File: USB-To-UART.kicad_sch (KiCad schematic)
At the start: 8 parts, among them Q1 NMOS, Q2 NMOS, U4 CH340X

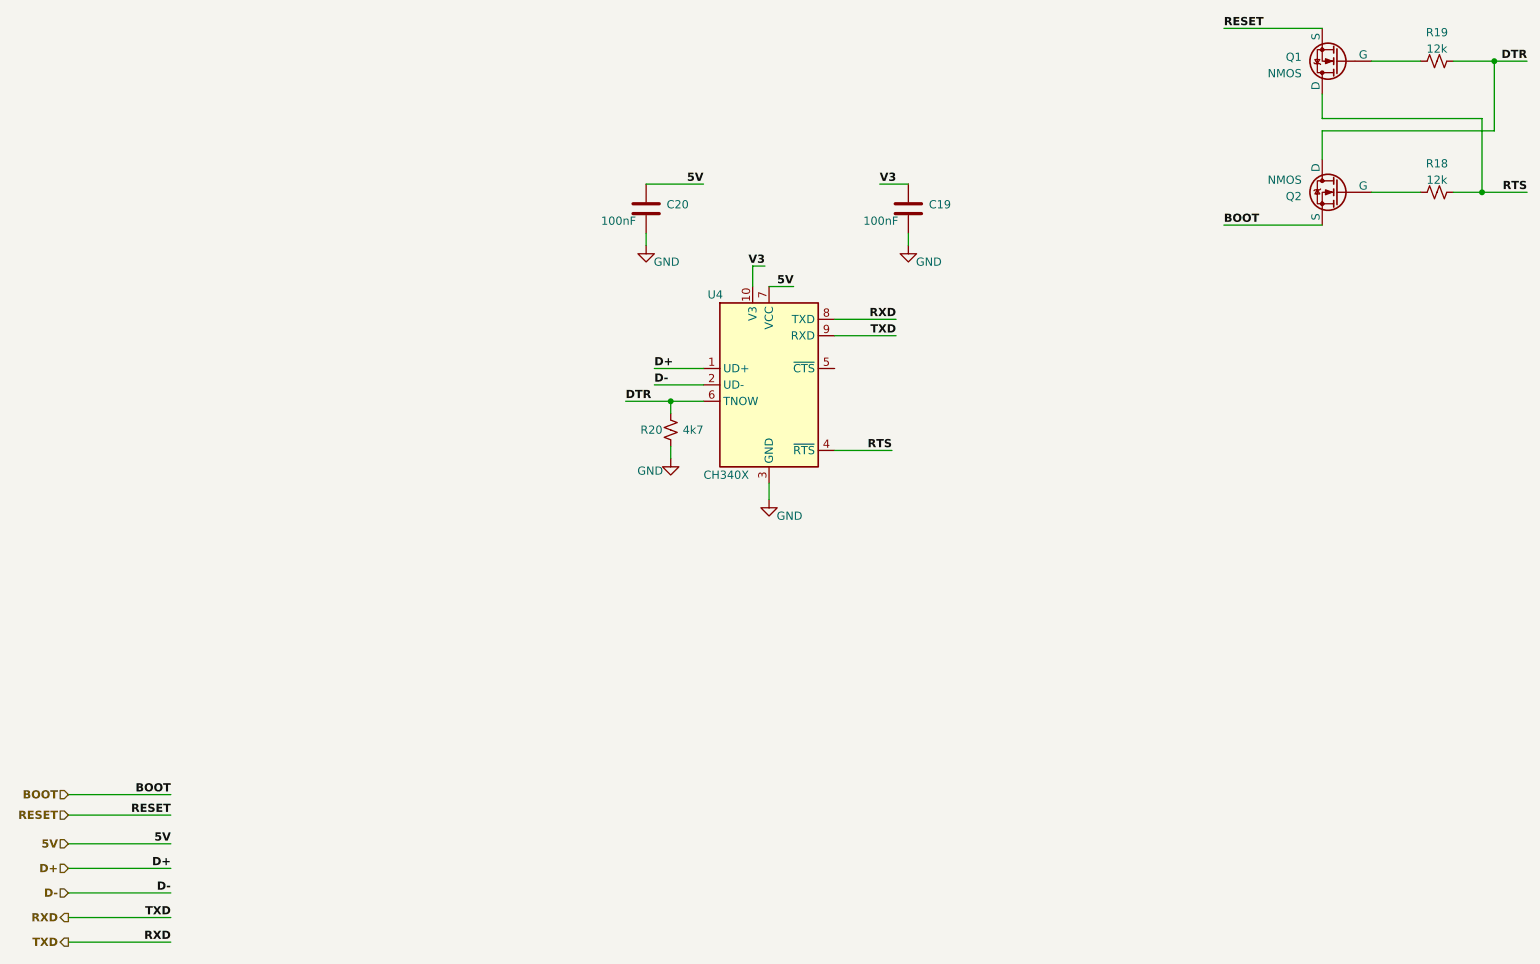
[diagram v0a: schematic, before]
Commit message: UART Tx and Rx correctly placed
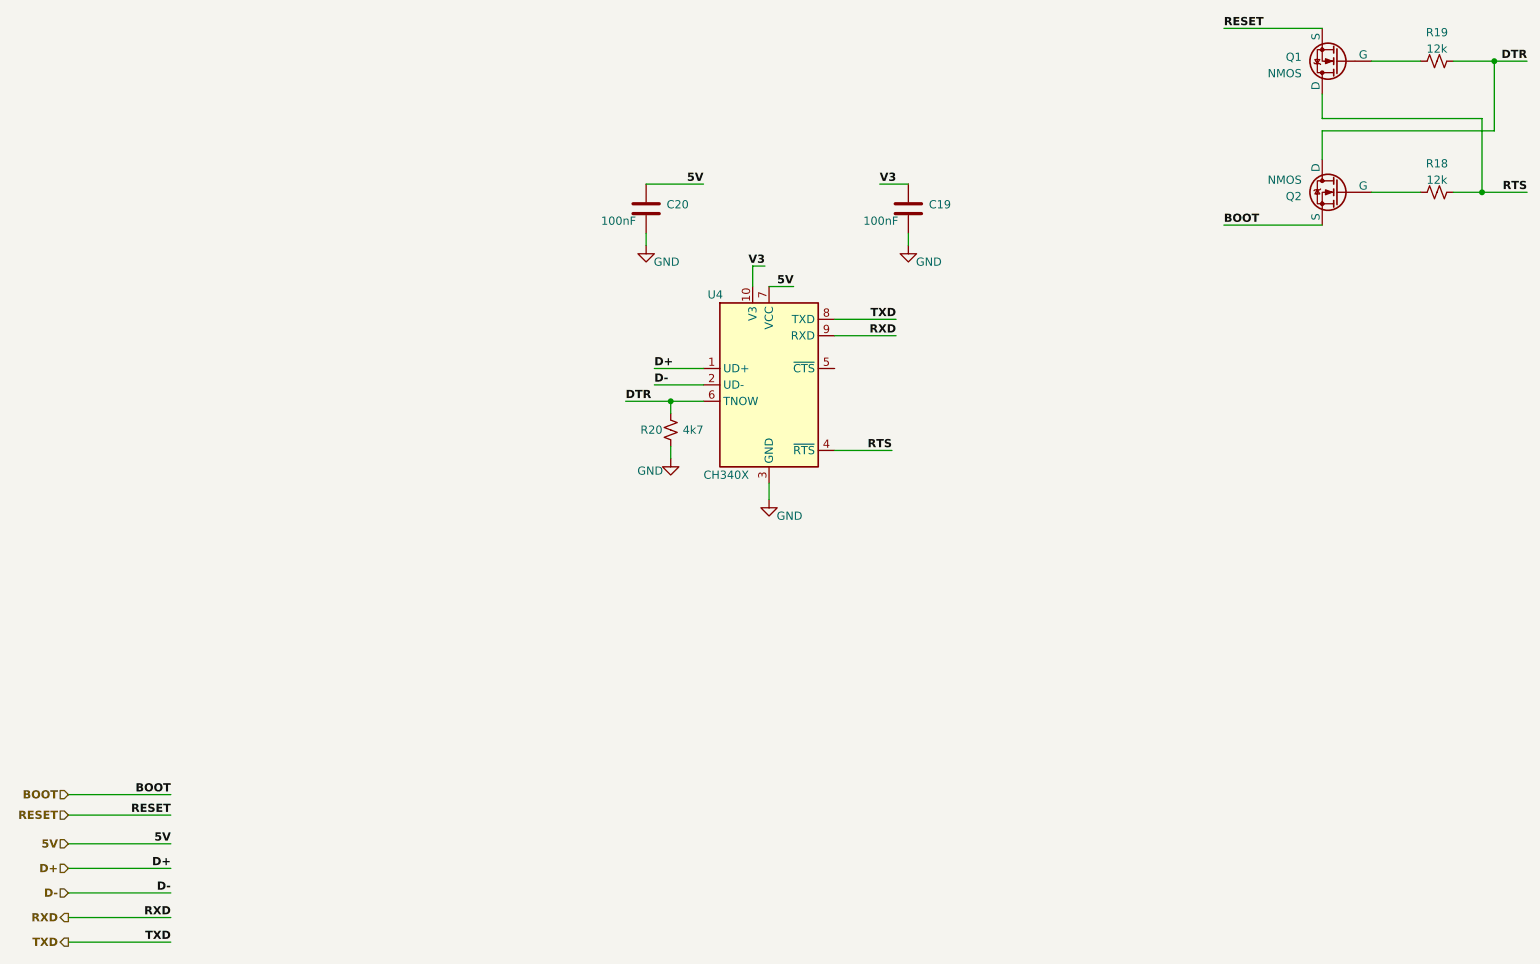
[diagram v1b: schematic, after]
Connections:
- net RXD: no longer U4.8 (TXD)
- new net TXD: U4.8 (TXD)
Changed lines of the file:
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@@
     (effects (font (size 1.27 1.27) (thickness 0.254) bold (color 255 0 0 1)) (justify left bottom))
   )
-  (label "TXD" (at 159.385 88.9 180) (fields_autoplaced)
+  (label "TXD" (at 159.385 86.36 180) (fields_autoplaced)
     (effects (font (size 1.27 1.27) bold (color 0 0 255 1)) (justify right bottom))
   )
@@
     (effects (font (size 1.27 1.27) bold (color 0 0 255 1)) (justify left bottom))
   )
-  (label "TXD" (at 46.99 179.07 180) (fields_autoplaced)
+  (label "TXD" (at 46.99 182.88 180) (fields_autoplaced)
     (effects (font (size 1.27 1.27) bold (color 0 0 255 1)) (justify right bottom))
   )
@@
     (effects (font (size 1.27 1.27) bold (color 0 0 255 1)) (justify left bottom))
   )
-  (label "RXD" (at 46.99 182.88 180) (fields_autoplaced)
+  (label "RXD" (at 46.99 179.07 180) (fields_autoplaced)
     (effects (font (size 1.27 1.27) bold (color 0 0 255 1)) (justify right bottom))
   )
-  (label "RXD" (at 159.385 86.36 180) (fields_autoplaced)
+  (label "RXD" (at 159.385 88.9 180) (fields_autoplaced)
     (effects (font (size 1.27 1.27) bold (color 0 0 255 1)) (justify right bottom))
   )

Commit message: Added Female Headers
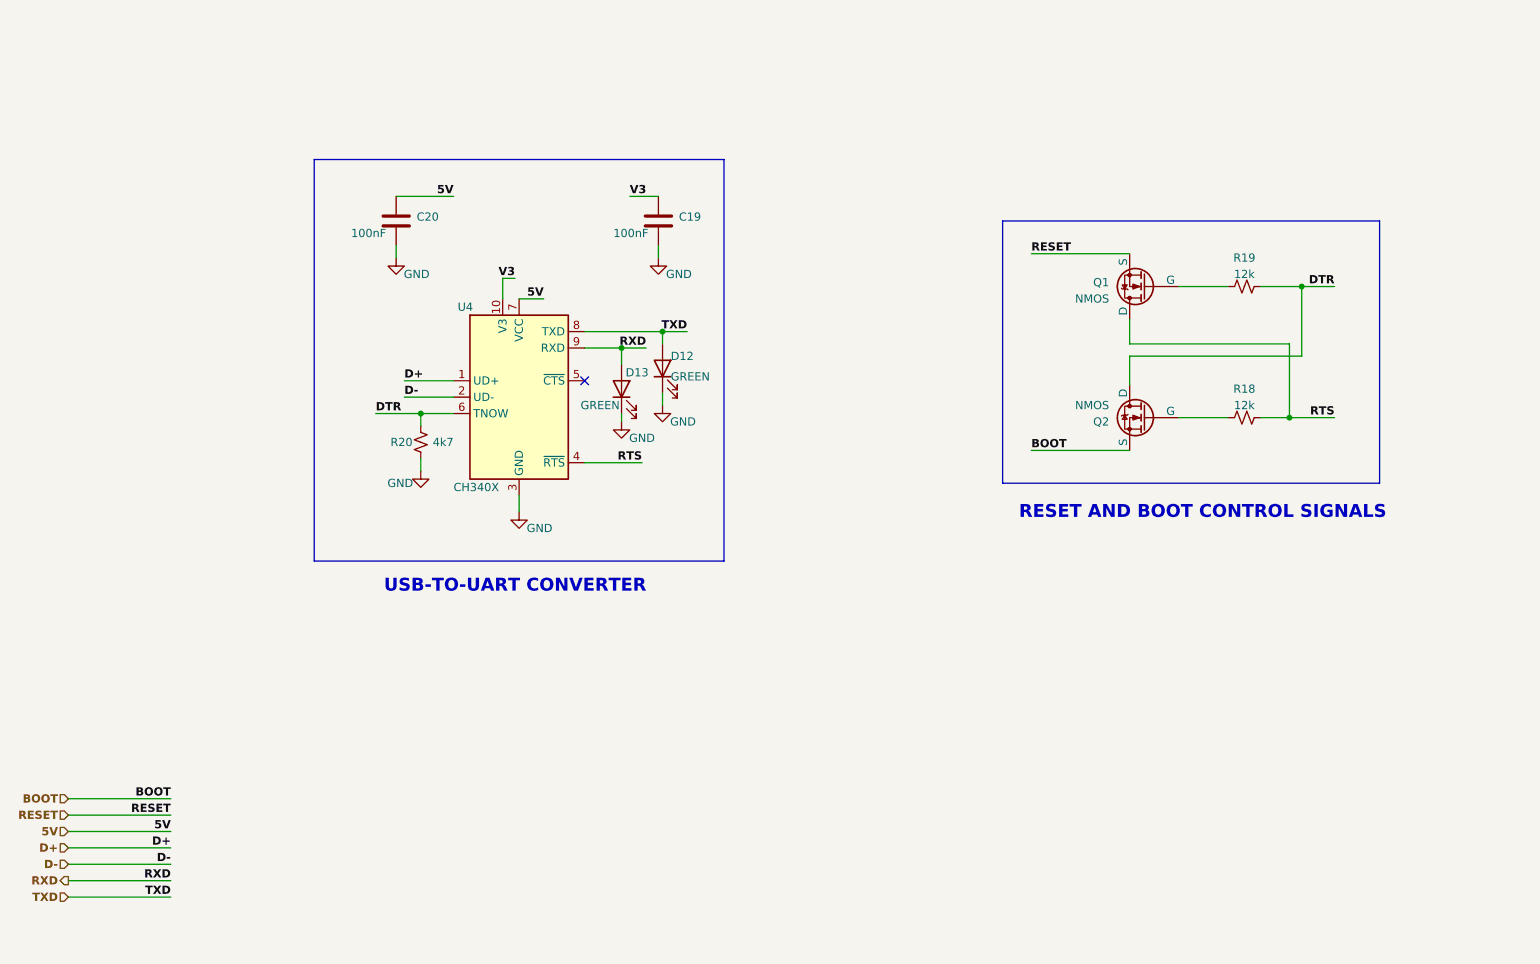
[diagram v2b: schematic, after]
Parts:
- added D12, D13: GREEN, symbol ESP32-S3_DB:LED
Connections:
- net GND: now also D12.1 (K), D13.1 (K)
- net RXD: now also D13.2 (A)
- net TXD: now also D12.2 (A)
- no-connect marks 0 -> 1
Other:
- note added: "RESET AND BOOT CONTROL SIGNALS"
- note added: "USB-TO-UART CONVERTER"
- moved on the sheet: C19, C20, Q1, Q2, R18, R19, R20, U4

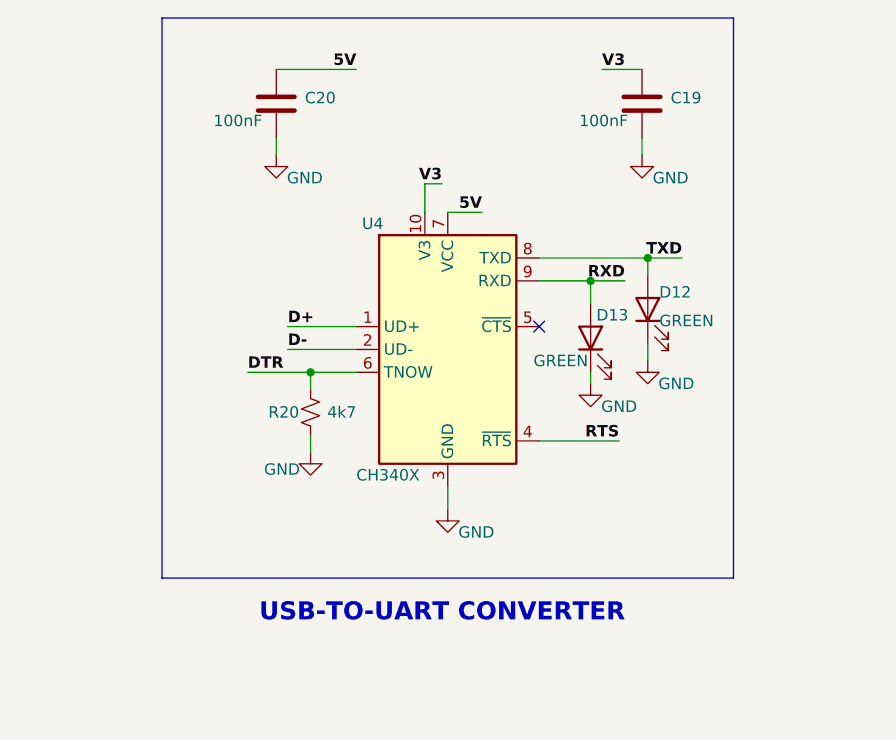
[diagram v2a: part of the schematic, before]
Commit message: Completed header connections
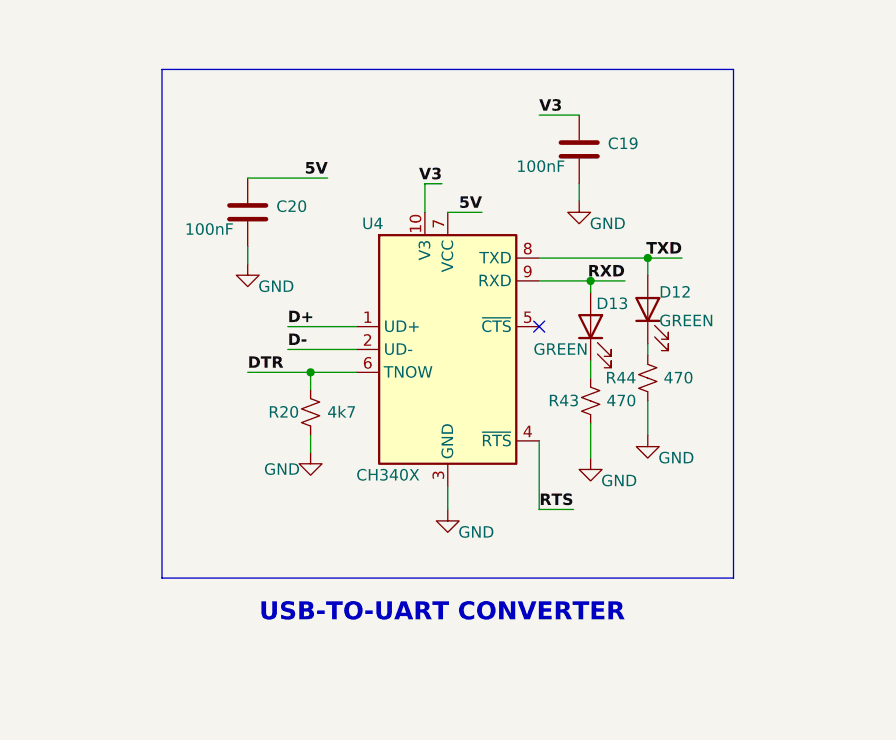
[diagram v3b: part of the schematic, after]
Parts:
- added R43, R44: 470, symbol ESP32-S3_DB:R_Small_US
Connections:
- net GND: now also R43.1, R44.1; no longer D12.1 (K), D13.1 (K)
- new net: D13.1 (K), R43.2
- new net: D12.1 (K), R44.2
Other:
- moved on the sheet: C19, C20, D13

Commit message: Assigned PN and Footprint for C
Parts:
- C19, C20: footprint (none) -> ESP32-S3_DB:C_0402_1005Metric; PN (none) -> EMK107B7104KAHT
- D12, D13: footprint (none) -> ESP32-S3_DB:LED_0603_1608Metric; PN (none) -> NCD0603C1
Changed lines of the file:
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@@
       (effects (font (size 1.27 1.27)) (justify right))
     )
-    (property "Footprint" "" (at 116.84 95.885 0)
+    (property "Footprint" "ESP32-S3_DB:LED_0603_1608Metric" (at 116.84 95.885 0)
       (effects (font (size 1.27 1.27)) hide)
     )
     (property "Datasheet" "~" (at 116.84 95.885 0)
+      (effects (font (size 1.27 1.27)) hide)
+    )
+    (property "PN" "NCD0603C1" (at 116.84 95.885 0)
       (effects (font (size 1.27 1.27)) hide)
     )
@@
       (effects (font (size 1.27 1.27)) (justify right))
     )
-    (property "Footprint" "" (at 114.6048 72.39 0)
+    (property "Footprint" "ESP32-S3_DB:C_0402_1005Metric" (at 114.6048 72.39 0)
       (effects (font (size 1.27 1.27)) hide)
     )
     (property "Datasheet" "~" (at 115.57 76.2 0)
+      (effects (font (size 1.27 1.27)) hide)
+    )
+    (property "PN" "EMK107B7104KAHT" (at 115.57 76.2 0)
       (effects (font (size 1.27 1.27)) hide)
     )
@@
       (effects (font (size 1.27 1.27)) (justify right))
     )
-    (property "Footprint" "" (at 77.7748 79.375 0)
+    (property "Footprint" "ESP32-S3_DB:C_0402_1005Metric" (at 77.7748 79.375 0)
       (effects (font (size 1.27 1.27)) hide)
     )
@@
       (effects (font (size 1.27 1.27)) hide)
     )
+    (property "PN" "EMK107B7104KAHT" (at 78.74 83.185 0)
+      (effects (font (size 1.27 1.27)) hide)
+    )
     (pin "1")
     (pin "2")
@@
       (effects (font (size 1.27 1.27)) (justify right))
     )
-    (property "Footprint" "" (at 123.19 93.98 0)
+    (property "Footprint" "ESP32-S3_DB:LED_0603_1608Metric" (at 123.19 93.98 0)
       (effects (font (size 1.27 1.27)) hide)
     )
@@
       (effects (font (size 1.27 1.27)) hide)
     )
+    (property "PN" "NCD0603C1" (at 123.19 93.98 0)
+      (effects (font (size 1.27 1.27)) hide)
+    )
